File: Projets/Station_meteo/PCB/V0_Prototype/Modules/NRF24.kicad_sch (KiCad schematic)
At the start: 19 parts, among them J27 132415, U8 NRF24L01

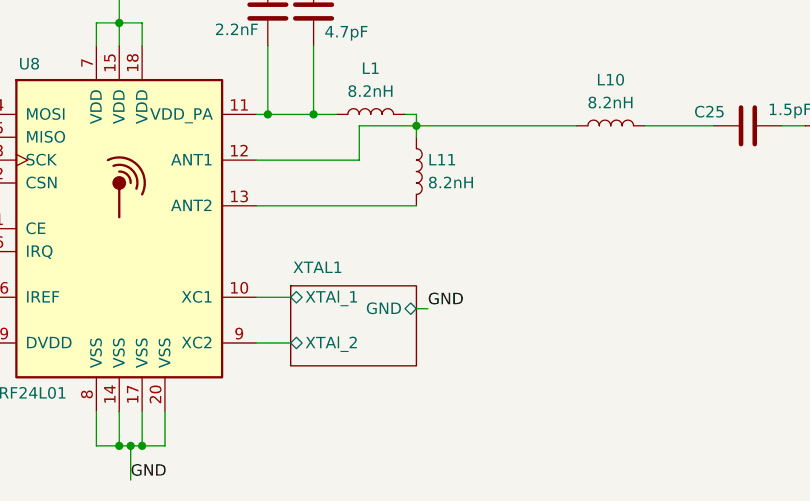
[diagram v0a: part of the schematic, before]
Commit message: Add V1 THT version
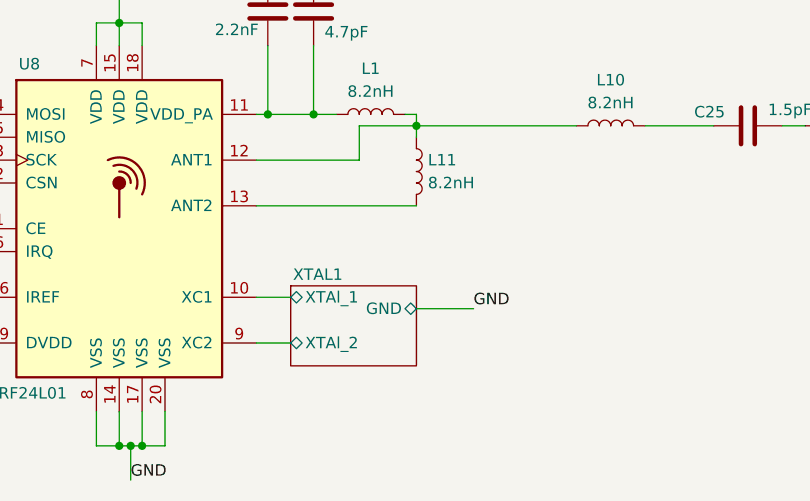
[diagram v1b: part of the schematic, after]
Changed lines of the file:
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@@
-	(wire
-		(pts
-			(xy 166.37 100.33) (xy 167.64 100.33)
-		)
-		(stroke
-			(width 0)
-			(type default)
-		)
-	)
 	(wire
 		(pts
@@
 		(pts
 			(xy 133.35 66.04) (xy 133.35 68.58)
+		)
+		(stroke
+			(width 0)
+			(type default)
+		)
+	)
+	(wire
+		(pts
+			(xy 166.37 100.33) (xy 172.72 100.33)
 		)
 		(stroke
@@
 	)
 	(label "GND"
-		(at 167.64 100.33 0)
+		(at 172.72 100.33 0)
 		(fields_autoplaced yes)
 		(effects
@@
 		)
 		(fill
-			(color 0 0 0 0.0000)
+			(color 24 24 143 0.2706)
 		)
 		(property "Sheetname" "XTAL1"
-			(at 152.654 96.52 0)
-			(effects
-				(font
+			(at 152.654 97.282 0)
+			(effects
+				(font
